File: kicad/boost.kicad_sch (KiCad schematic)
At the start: 17 parts, among them U5 TPS61391RTER

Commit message: library cleanup
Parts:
- U5: symbol New_Library:TPS61391RTER -> NewSymbols:TPS61391RTER
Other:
- title: NUMITRON CONTROL -> BOOST CONVERTER
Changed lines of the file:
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@@
 	(paper "USLetter")
 	(title_block
-		(title "NUMITRON CONTROL")
+		(title "BOOST CONVERTER")
 		(rev "0")
 	)
@@
 	)
 	(symbol
-		(lib_id "New_Library:TPS61391RTER")
+		(lib_id "NewSymbols:TPS61391RTER")
 		(at 127 101.6 0)
 		(unit 1)

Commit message: began pcb layout
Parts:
- Capd1, Ccap1, Cin1: footprint (none) -> Capacitor_SMD:C_0402_1005Metric
- Cavcc1, Cout1: footprint (none) -> Capacitor_SMD:C_0603_1608Metric
- Cmon1, Cmon2: footprint (none) -> Capacitor_SMD:C_0201_0603Metric
- D1: footprint (none) -> Diode_SMD:D_SOD-123
- L1: footprint (none) -> Inductor_SMD:L_1008_2520Metric
- Ren1, Rfbb1, Risshort1, Rmon1, Rmon2, Rvcc1: footprint (none) -> Resistor_SMD:R_0402_1005Metric
- Rfbt1: footprint (none) -> Resistor_SMD:R_0603_1608Metric
- U5: footprint RTE0016C -> NewFootprints:RTE0016C
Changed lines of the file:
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@@
 			)
 		)
-		(property "Footprint" ""
+		(property "Footprint" "Resistor_SMD:R_0402_1005Metric"
 			(at 191.516 127.254 90)
 			(effects
@@
 			)
 		)
-		(property "Footprint" ""
+		(property "Footprint" "Capacitor_SMD:C_0402_1005Metric"
 			(at 77.1652 130.81 0)
 			(effects
@@
 			)
 		)
-		(property "Footprint" ""
+		(property "Footprint" "Inductor_SMD:L_1008_2520Metric"
 			(at 127 63.5 0)
 			(effects
@@
 			)
 		)
-		(property "Footprint" ""
+		(property "Footprint" "Capacitor_SMD:C_0603_1608Metric"
 			(at 229.5652 130.81 0)
 			(effects
@@
 			)
 		)
-		(property "Footprint" "RTE0016C"
+		(property "Footprint" "NewFootprints:RTE0016C"
 			(at 127 101.6 0)
 			(effects
@@
 			)
 		)
-		(property "Datasheet" "TPS61391RTER"
+		(property "Datasheet" "https://www.ti.com/lit/ds/symlink/tps61391.pdf?HQS=dis-dk-null-digikeymode-dsf-pf-null-wwe&ts=1725979079375&ref_url=https%253A%252F%252Fwww.ti.com%252Fgeneral%252Fdocs%252Fsuppproductinfo.tsp%253FdistId%253D10%2526gotoUrl%253Dhttps%253A%252F%252Fwww.ti.com%252Flit%252Fgpn%252Ftps61391"
 			(at 127 101.6 0)
 			(effects
@@
 			)
 		)
-		(property "Footprint" ""
+		(property "Footprint" "Capacitor_SMD:C_0201_0603Metric"
 			(at 178.7652 130.81 0)
 			(effects
@@
 			)
 		)
-		(property "Footprint" ""
+		(property "Footprint" "Resistor_SMD:R_0402_1005Metric"
 			(at 89.916 127.254 90)
 			(effects
@@
 			)
 		)
-		(property "Footprint" ""
+		(property "Footprint" "Resistor_SMD:R_0402_1005Metric"
 			(at 166.116 127.254 90)
 			(effects
@@
 			)
 		)
-		(property "Footprint" ""
+		(property "Footprint" "Resistor_SMD:R_0402_1005Metric"
 			(at 64.516 76.454 90)
 			(effects
@@
 			)
 		)
-		(property "Footprint" ""
+		(property "Footprint" "Capacitor_SMD:C_0603_1608Metric"
 			(at 64.4652 130.81 0)
 			(effects
@@
 			)
 		)
-		(property "Footprint" ""
+		(property "Footprint" "Capacitor_SMD:C_0402_1005Metric"
 			(at 51.7652 130.81 0)
 			(effects
@@
 			)
 		)
-		(property "Footprint" ""
+		(property "Footprint" "Capacitor_SMD:C_0402_1005Metric"
 			(at 39.0652 130.81 0)
 			(effects
@@
 			)
 		)
-		(property "Footprint" ""
+		(property "Footprint" "Diode_SMD:D_SOD-123"
 			(at 177.8 63.5 0)
 			(effects
@@
 			)
 		)
-		(property "Footprint" ""
+		(property "Footprint" "Resistor_SMD:R_0402_1005Metric"
 			(at 216.916 101.854 90)
 			(effects
@@
 			)
 		)
-		(property "Footprint" ""
+		(property "Footprint" "Resistor_SMD:R_0603_1608Metric"
 			(at 216.916 76.454 90)
 			(effects
@@
 			)
 		)
-		(property "Footprint" ""
+		(property "Footprint" "Capacitor_SMD:C_0201_0603Metric"
 			(at 204.1652 130.81 0)
 			(effects
@@
 			)
 		)
-		(property "Footprint" ""
+		(property "Footprint" "Resistor_SMD:R_0402_1005Metric"
 			(at 51.816 76.454 90)
 			(effects

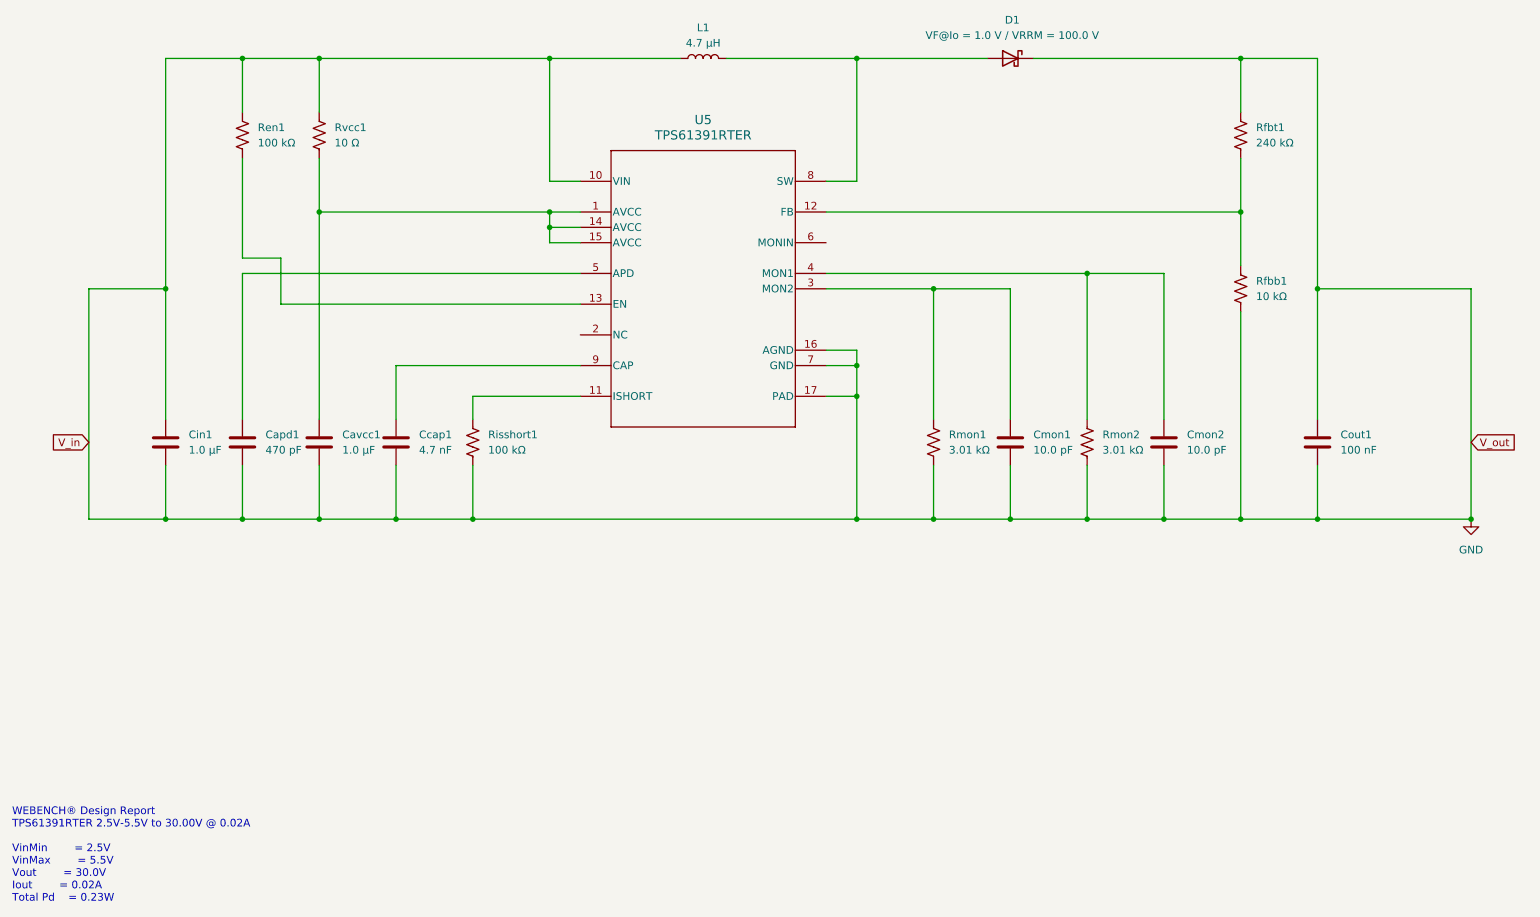
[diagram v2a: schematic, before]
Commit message: boost converter refactor
new design from web bench to reduce bom complexity & increase efficiency
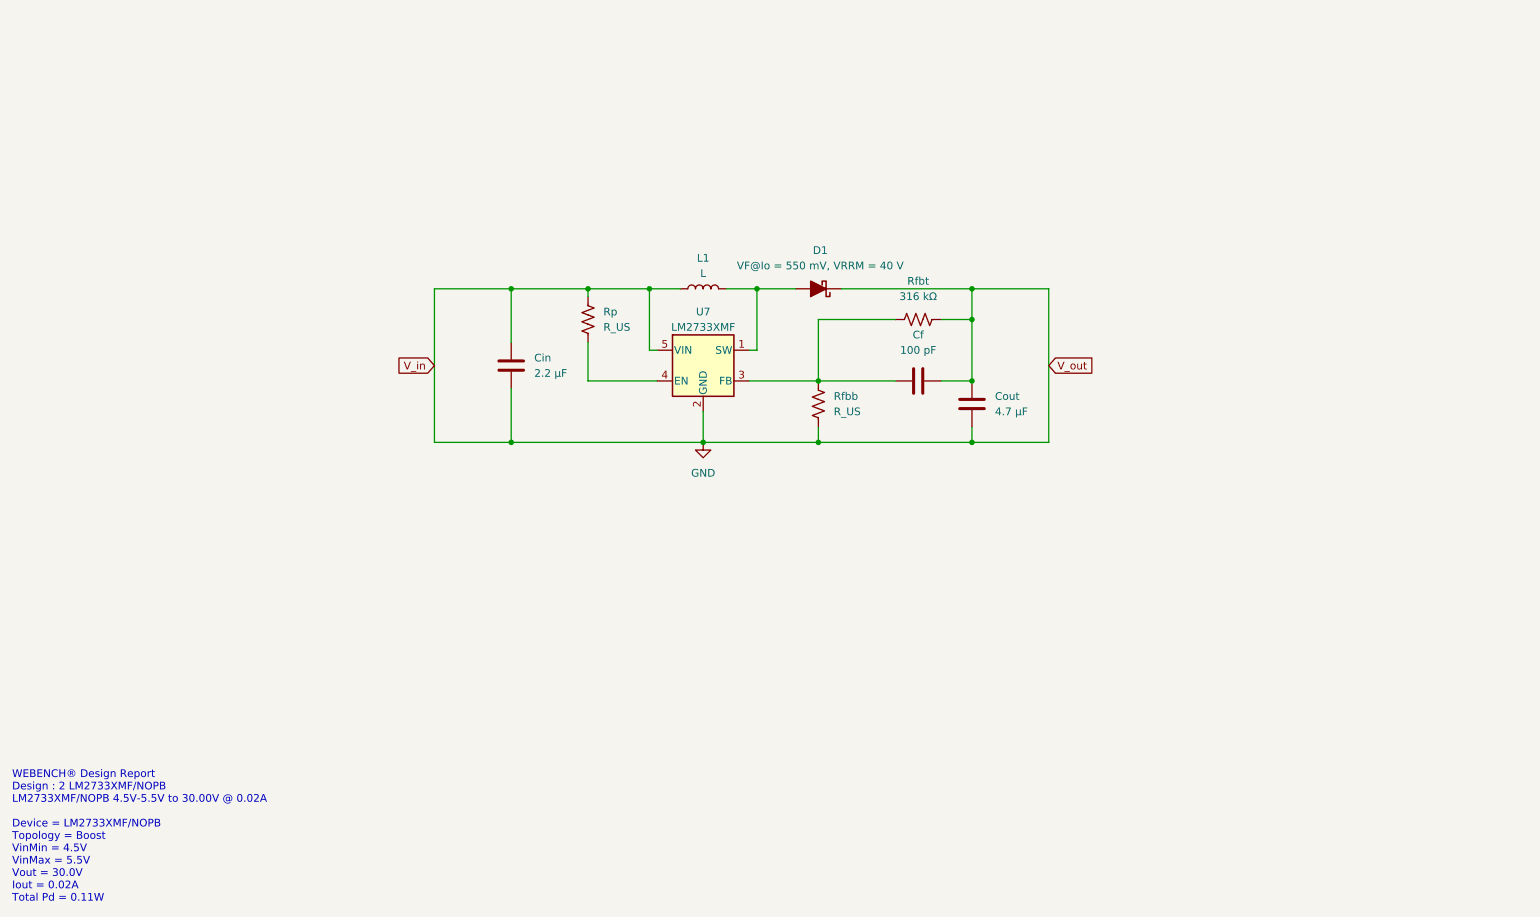
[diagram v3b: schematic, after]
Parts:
- removed Capd1: 470 pF, Capacitor_SMD:C_0402_1005Metric, symbol Device:C
- removed Cavcc1: 1.0 μF, Capacitor_SMD:C_0603_1608Metric, symbol Device:C
- removed Ccap1: 4.7 nF, Capacitor_SMD:C_0402_1005Metric, symbol Device:C
- removed Cin1: 1.0 μF, Capacitor_SMD:C_0402_1005Metric, symbol Device:C
- removed Cmon1, Cmon2: 10.0 pF, Capacitor_SMD:C_0201_0603Metric, symbol Device:C
- removed Cout1: 100 nF, Capacitor_SMD:C_0603_1608Metric, symbol Device:C
- removed D1: VF@Io = 1.0 V / VRRM = 100.0 V, Diode_SMD:D_SOD-123, symbol Device:D_Schottky
- removed Ren1, Risshort1: 100 kΩ, Resistor_SMD:R_0402_1005Metric, symbol Device:R_US
- removed Rfbb1: 10 kΩ, Resistor_SMD:R_0402_1005Metric, symbol Device:R_US
- removed Rfbt1: 240 kΩ, Resistor_SMD:R_0603_1608Metric, symbol Device:R_US
- removed Rmon1, Rmon2: 3.01 kΩ, Resistor_SMD:R_0402_1005Metric, symbol Device:R_US
- removed Rvcc1: 10 Ω, Resistor_SMD:R_0402_1005Metric, symbol Device:R_US
- removed U5: TPS61391RTER, NewFootprints:RTE0016C, symbol NewSymbols:TPS61391RTER
- added Cf: 100 pF, symbol Device:C
- added Cin: 2.2 μF, symbol Device:C
- added Cout: 4.7 μF, symbol Device:C
- added D1: VF@Io = 550 mV, VRRM = 40 V, symbol Device:D_Schottky_Filled
- added Rfbb, Rp: R_US, symbol Device:R_US
- added Rfbt: 316 kΩ, symbol Device:R_US
- added U7: LM2733XMF, Package_TO_SOT_SMD:SOT-23-5, symbol Regulator_Switching:LM2733XMF
- L1: value 4.7 μH -> L; footprint Inductor_SMD:L_1008_2520Metric -> (none)
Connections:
- net GND: now also Cf.2, Cin.1, Cin.2, Cout.1, Cout.2, D1.1 (K), Rfbb.2, Rfbt.2, Rp.1, U7.2 (GND), U7.5 (VIN)
- net at L1.2: now also D1.2 (A), U7.1 (SW)
- new net: Cf.1, Rfbb.1, Rfbt.1, U7.3 (FB)
- new net: Rp.2, U7.4 (EN)
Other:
- note added: "WEBENCH® Design Report Design : 2 LM2733XMF/NOPB LM2733XMF/NOPB 4.5V-5.5V to 30.00V @ 0.02A Device = LM2733XMF/NOPB Topology = Boost VinMin = 4.5V VinMax = 5.5V Vout = 30.0V Iout = 0.02A Total Pd = 0.11W"
- note removed: "WEBENCH® Design Report TPS61391RTER 2.5V-5.5V to 30.00V @ 0.02A VinMin = 2.5V VinMax = 5.5V Vout = 30.0V Iout = 0.02A Total Pd = 0.23W"
